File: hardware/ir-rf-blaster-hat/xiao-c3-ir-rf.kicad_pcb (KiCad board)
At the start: 4 copper layers, 23 x 50 mm, 16 parts, among them J1 XIAO_L, J2 XIAO_R, M1 CC1101, Q1 AO3400A

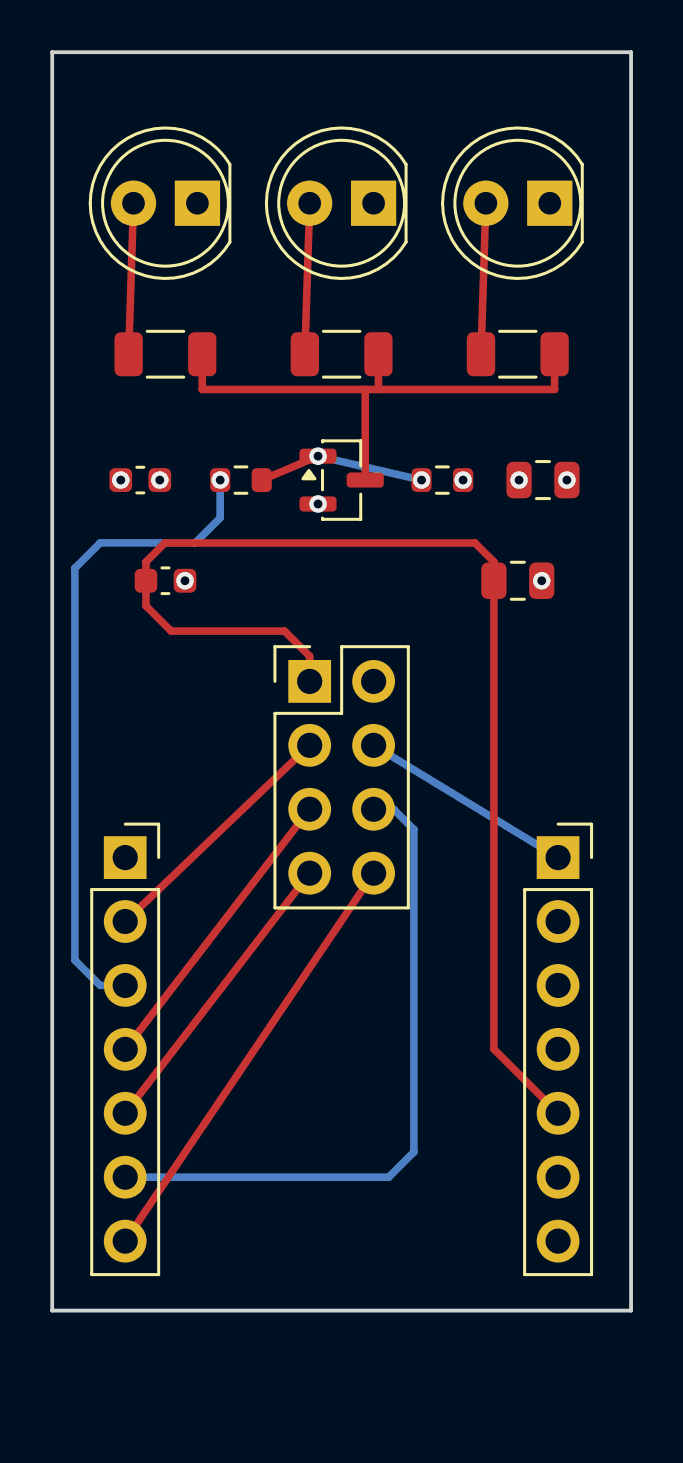
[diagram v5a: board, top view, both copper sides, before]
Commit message: feat(hardware): re-layout IR/RF blaster — back-side E07 CC1101, USB-west XIAO
Rework the XIAO IR+RF blaster hat per design review:

- XIAO rotated horizontal so USB-C exits the WEST edge; LEDs stay north.
- CC1101 moved to the BACK on a swappable 2x04 FEMALE socket (band-agnostic);
  E07-M1101D module body lies over the XIAO back, SMA/antenna off the SOUTH edge.
- Socket wired to the FIXED E07-M1101D datasheet pinout (1 GND 2 VCC 3 GDO0 4 CSN
  5 SCK 6 MOSI 7 MISO 8 GDO2) — no more generic placeholder; module plugs straight in.
- SPI fan split N-row-from-J1 / S-row-from-J2 so no trace clips the dense pad block.
- All-layer antenna keepout under the RF region; board now 23 x 54 mm.
- DRC 0 errors / 0 unconnected; regenerated gerbers + top/bottom renders + an
  orientation diagram. README documents 433 MHz E07 + the band-agnostic swap.

Co-Authored-By: Claude Opus 4.8 <noreply@anthropic.com>
Claude-Session: https://claude.ai/code/session_01NfkRErMrPyNuft1RbpzMet
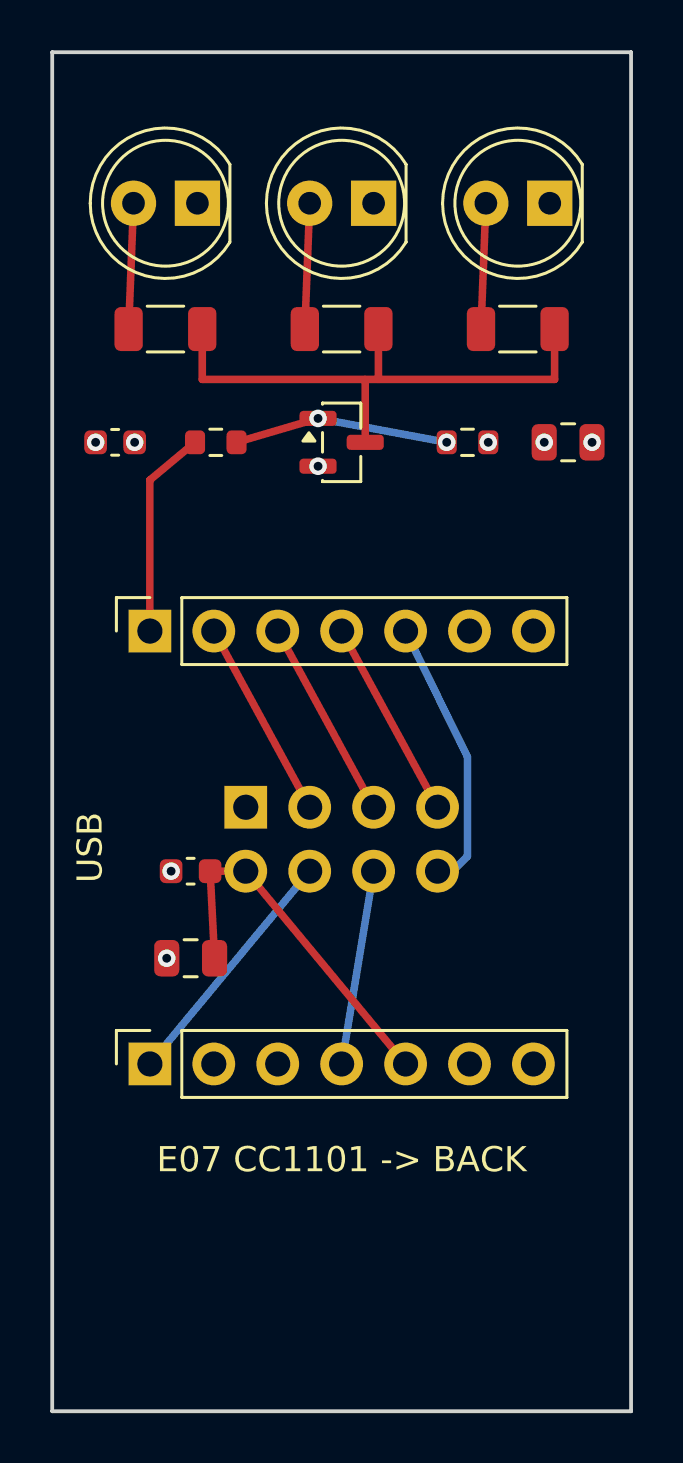
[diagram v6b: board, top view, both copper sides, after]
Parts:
- J1: value XIAO_L -> XIAO_top
- J2: value XIAO_R -> XIAO_bot
- M1: value CC1101 -> E07-M1101D; footprint PinHeader_2x04_P2.54mm_Vertical -> PinSocket_2x04_P2.54mm_Vertical; moved to B.Cu
- moved C4 19.8 mm to (5.50, 36.0), turned to 180 degrees
- moved J2 18.2 mm to (3.88, 40.2), turned to 90 degrees
- moved C3 11.6 mm to (5.50, 32.5), turned to 180 degrees
- moved J1 9.05 mm to (3.88, 23.0), turned to 90 degrees
- moved M1 5.61 mm to (7.69, 30.0), turned to 90 degrees
- moved C1 1.80 mm to (2.50, 15.5)
- moved C2 1.80 mm to (20.5, 15.5)
- moved R4 1.80 mm to (6.50, 15.5)
- moved R5 1.80 mm to (16.5, 15.5)
- moved Q1 1.50 mm to (11.5, 15.5)
- moved R1 1.00 mm to (4.50, 11.0)
- moved R2 1.00 mm to (11.5, 11.0)
- moved R3 1.00 mm to (18.5, 11.0)
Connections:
- J1 pad 1: GND -> IR_TX
- J1 pad 2: CC_GDO2 -> CC_GDO0
- J1 pad 3: IR_TX -> CC_SCK
- J1 pad 4: CC_CSN -> CC_MISO
- J1 pad 5: CC_GDO0 -> CC_GDO2
- J1 pad 6: CC_SCK -> (no net)
- J1 pad 7: CC_MOSI -> (no net)
- J2 pad 1: CC_MISO -> CC_CSN
- J2 pad 2: GND -> (no net)
- J2 pad 3: GND -> (no net)
- J2 pad 4: GND -> CC_MOSI
- M1 pad 1: +3V3 -> GND
- M1 pad 2: GND -> +3V3
- M1 pad 3: CC_GDO2 -> CC_GDO0
- M1 pad 4: CC_MISO -> CC_CSN
- M1 pad 5: CC_CSN -> CC_SCK
- M1 pad 6: CC_SCK -> CC_MOSI
- M1 pad 7: CC_GDO0 -> CC_MISO
- M1 pad 8: CC_MOSI -> CC_GDO2
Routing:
- net +3V3: track 47.5 -> 14.8 mm
- net CC_SCK: track 26.6 -> 7.97 mm
- net IR_TX: track 26.1 -> 8.34 mm, vias 1 -> 0
- net CC_MOSI: track 17.6 -> 7.76 mm
- net CC_GDO0: track 12.0 -> 7.97 mm
- net CC_CSN: track 12.0 -> 9.95 mm
- net Q_GATE: track 6.65 -> 8.57 mm
- net LED3_K: track 6.00 -> 5.00 mm
- net LED2_K: track 6.00 -> 5.00 mm
- net LED1_K: track 6.00 -> 5.00 mm
- net CC_GDO2: track 10.1 -> 11.0 mm
- net Q_DRAIN: track 21.8 -> 22.5 mm
- net CC_MISO: track 8.58 -> 7.97 mm
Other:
- board size 23 x 50 mm -> 23 x 54 mm
- board text added: "ANT v"
- board text added: "E07 CC1101 -> BACK"
- board text added: "USB"

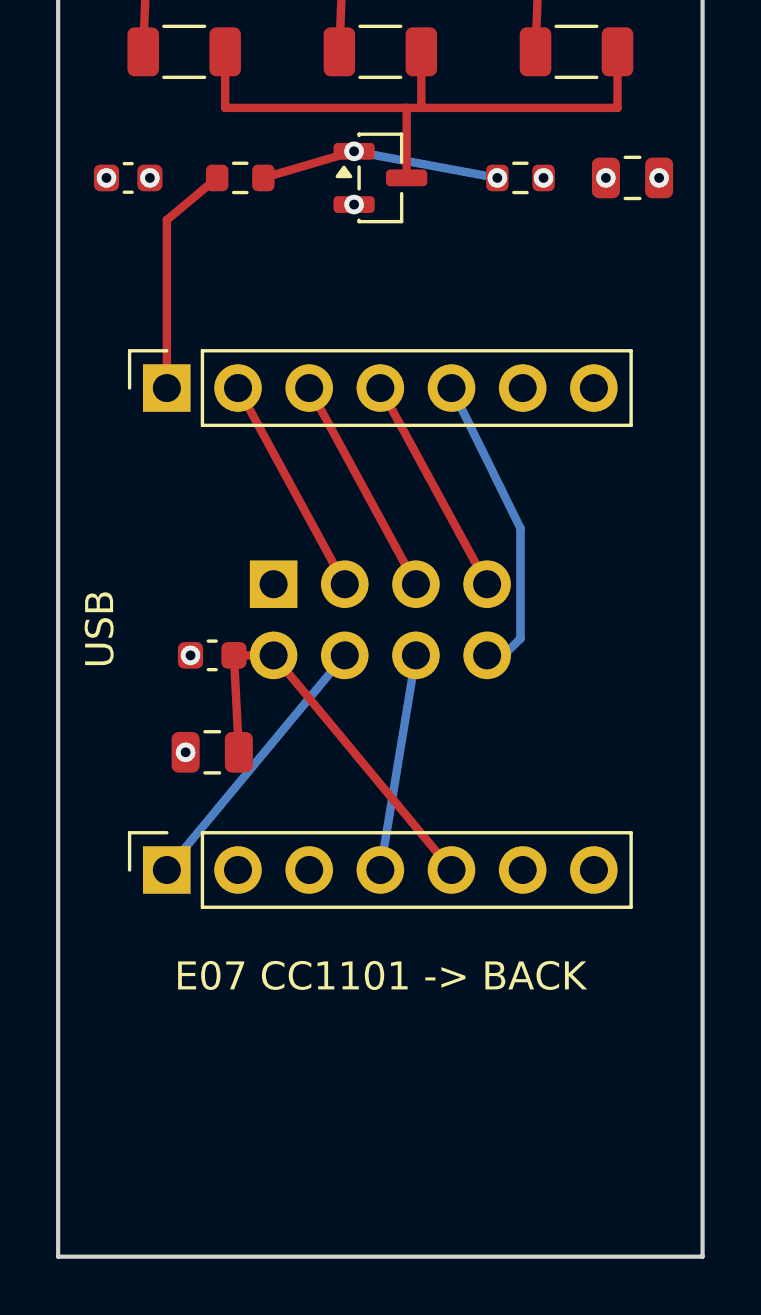
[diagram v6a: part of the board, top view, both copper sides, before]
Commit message: feat(hardware): swap in official Seeed XIAO-ESP32-C3-DIP footprint
Replace the provisional two 1x7 sockets with Seeed's official XIAO-ESP32-C3-DIP
footprint (from the wiki KiCad library):

- Real 15.24 mm row pitch (was a provisional 17.2 mm), hybrid SMD+THT castellated
  pads, rot180 so USB-C exits the west edge.
- Re-derived the whole fan around the authoritative pad map (power on pads 12/13/14
  = 3V3/GND/5V; strapping D0/D8/D9 kept off critical lines). E07 north row fed from
  the XIAO north row, south row from the south, MISO on a clean east-side dogleg.
- 3V3 decaps relocated to the front south strip; IR_TX gets its F.Cu<->B.Cu via.
- Vendor footprint's own silk stripped (it overhangs the USB end + crosses its
  castellated pads); pads + our labels remain.
- DRC 0/0, reproducible from the committed generator + footprints. Regenerated
  board, gerbers, top/bottom renders. README pin map + BOM updated; standoff
  (~1 mm pin protrusion) confirmed clear.

Co-Authored-By: Claude Opus 4.8 <noreply@anthropic.com>
Claude-Session: https://claude.ai/code/session_01NfkRErMrPyNuft1RbpzMet
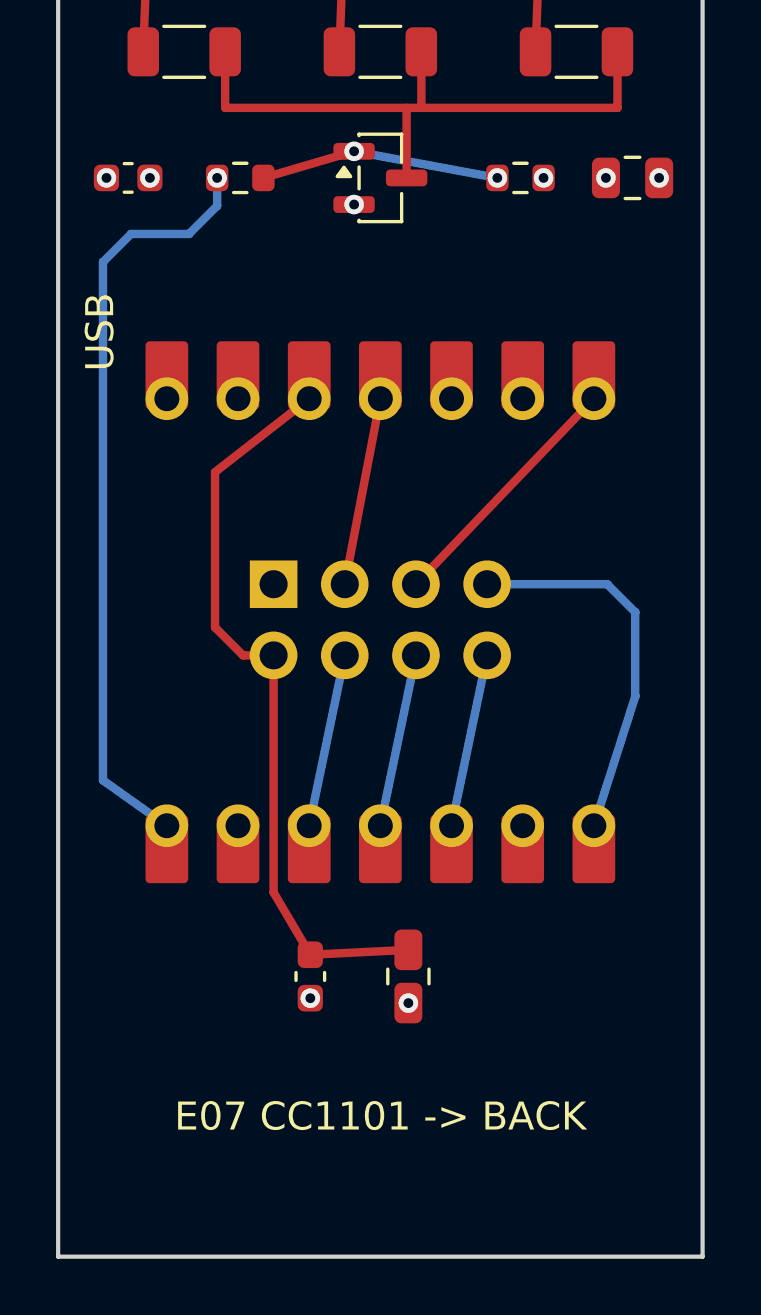
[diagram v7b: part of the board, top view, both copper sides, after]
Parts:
- removed J1: XIAO_top, PinSocket_1x07_P2.54mm_Vertical
- removed J2: XIAO_bot, PinSocket_1x07_P2.54mm_Vertical
- added A1: XIAO_ESP32C3, XIAO-ESP32-C3-DIP, F.Cu at (11.5, 31.0)
- moved C3 12.0 mm to (9.00, 44.0), turned to -90 degrees
- moved C4 10.6 mm to (12.5, 44.0), turned to -90 degrees
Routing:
- net IR_TX: track 8.34 -> 27.2 mm, vias 0 -> 1
- net +3V3: track 14.8 -> 26.9 mm
- net CC_MISO: track 7.97 -> 13.6 mm
- net CC_GDO2: track 11.0 -> 6.21 mm
- net CC_CSN: track 9.95 -> 6.21 mm
- net CC_MOSI: track 7.76 -> 6.21 mm
- net CC_GDO0: track 7.97 -> 6.74 mm
- net CC_SCK: track 7.97 -> 9.17 mm

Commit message: fix(hardware): correct IR LED polarity (pad1 is cathode)
The LED_D5.0mm footprint's pad 1 (square, flat-silk side) is the CATHODE, but the
generator wired pad 1 to +5V -> the LEDs were reverse-biased (passes DRC, never
lights). Swap so pad 1 = LED_K (-> current-limit R -> MOSFET) and pad 2 = anode =
+5V, and place the LEDs rot0 (offset -1.27) so the cathode sits west toward the
resistor (straight cathode traces). Verified: D1-3 pad1=LEDn_K, pad2=+5V; Q1
AO3400A SOT-23 confirmed 1=Gate/2=Source(GND)/3=Drain. DRC still 0/0. README gains
a hand-solder polarity note.

Co-Authored-By: Claude Opus 4.8 <noreply@anthropic.com>
Claude-Session: https://claude.ai/code/session_01NfkRErMrPyNuft1RbpzMet
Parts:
- moved D1 2.54 mm to (3.23, 6.00), turned to 0 degrees
- moved D2 2.54 mm to (10.2, 6.00), turned to 0 degrees
- moved D3 2.54 mm to (17.2, 6.00), turned to 0 degrees
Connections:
- D1 pad 1: +5V -> LED1_K
- D1 pad 2: LED1_K -> +5V
- D2 pad 1: +5V -> LED2_K
- D2 pad 2: LED2_K -> +5V
- D3 pad 1: +5V -> LED3_K
- D3 pad 2: LED3_K -> +5V
